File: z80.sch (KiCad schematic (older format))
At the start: 24 parts, among them J3 Conn_02x20_Odd_Even, J5 USB_B, J6 PWR, SW1 KS01Q, U1 Z80CPU, U2 74AHC14, U3 SST39SF010, U4 74AHC32, U5 AS6C1008-55PCN, U6 74AHC138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

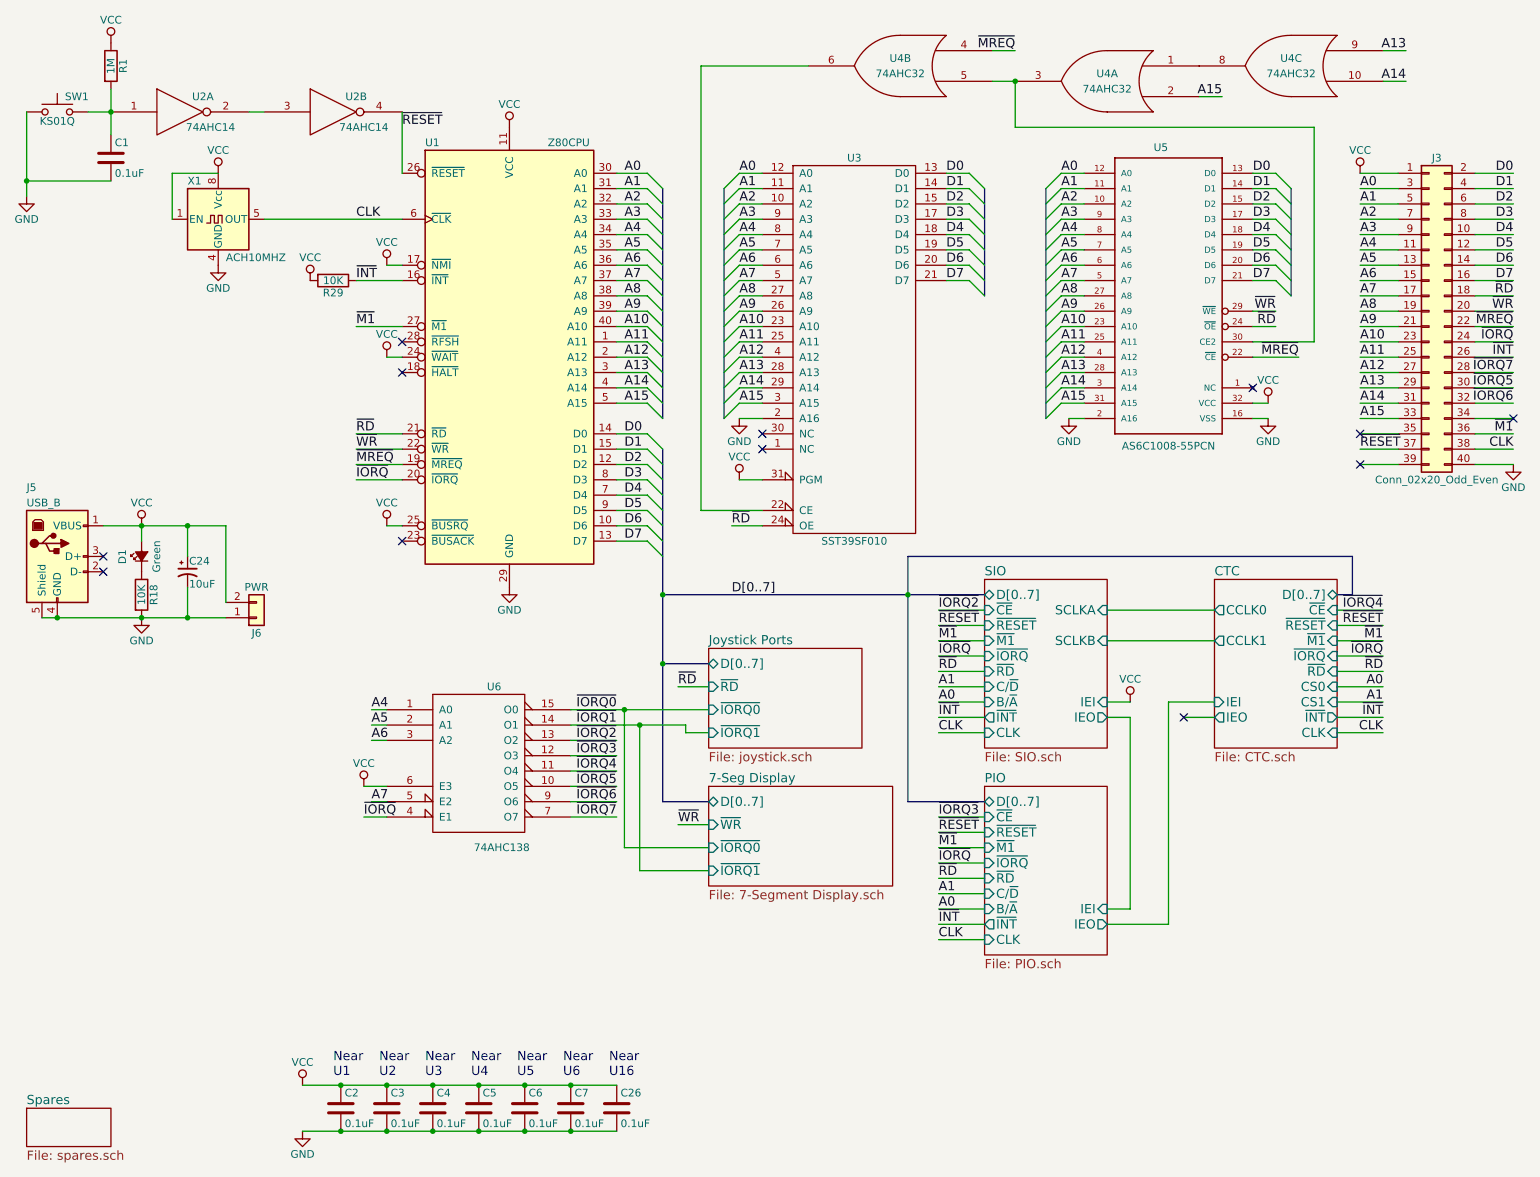
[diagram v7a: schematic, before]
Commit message: Schematic for an LCD panel interface circuit.
git-svn-id: svn+ssh://dev.thehead.ca/depot/main/z80@632 995eaefb-0ce2-40e3-b8bc-69bf8729875b
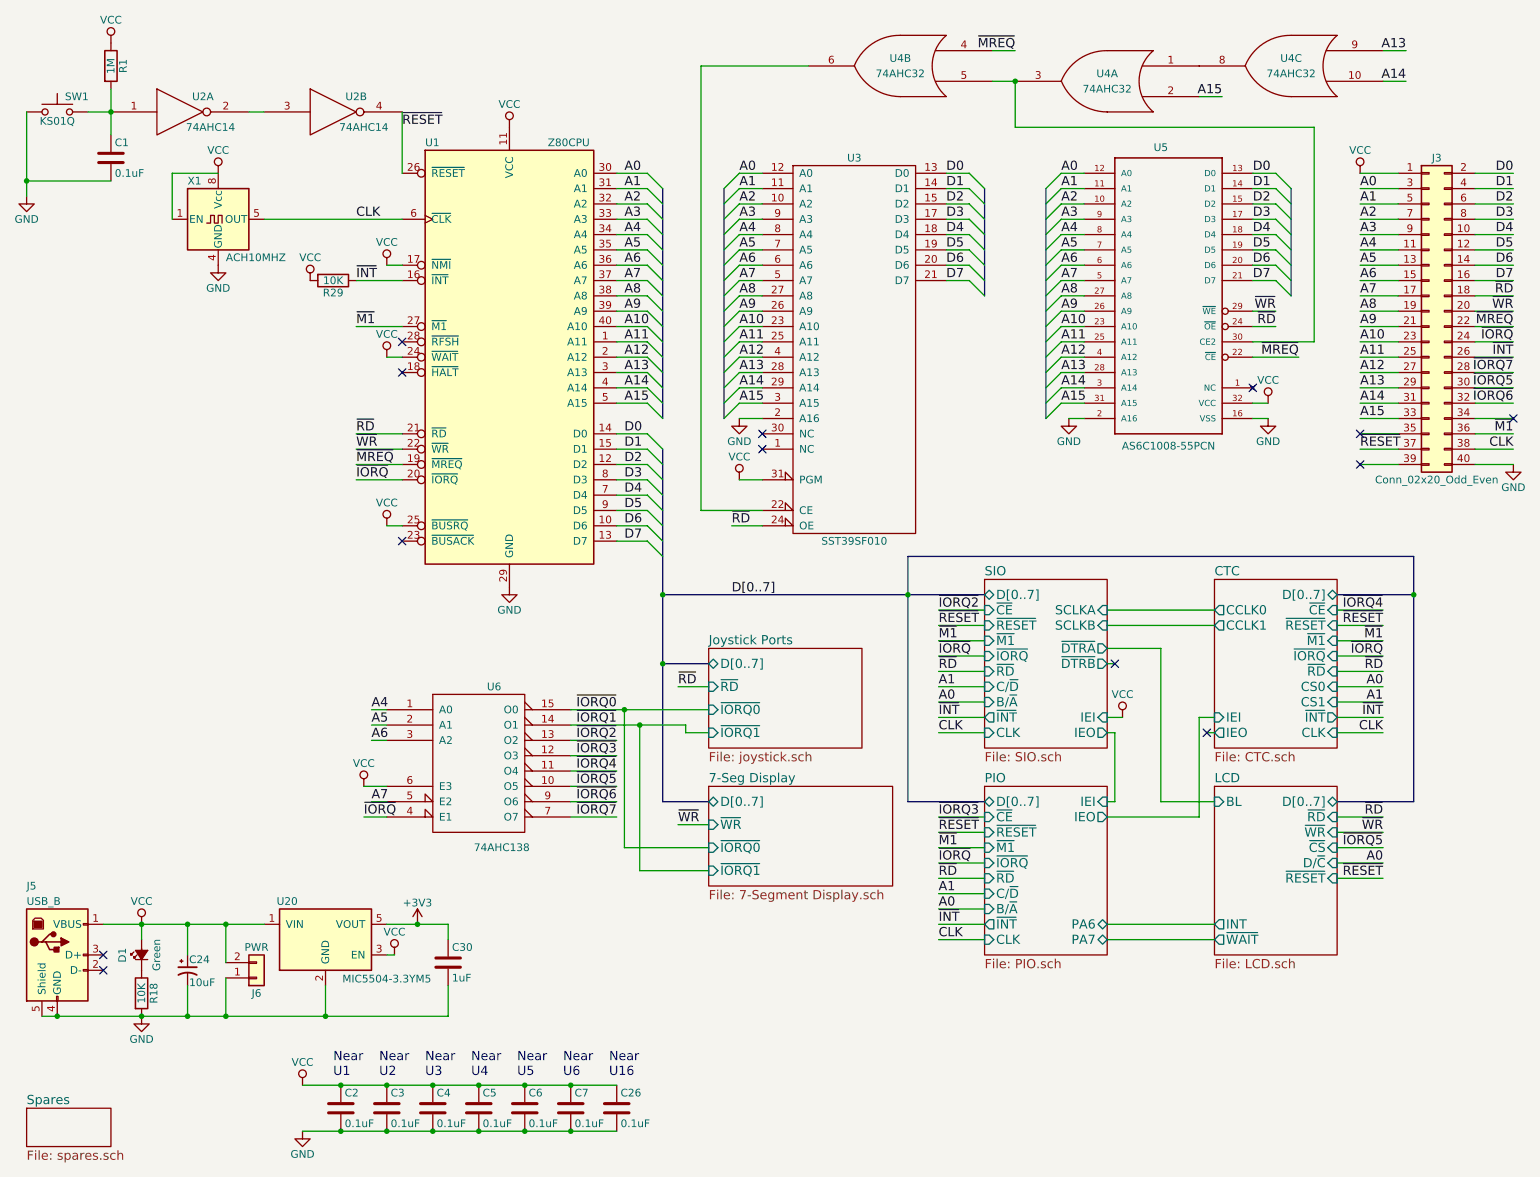
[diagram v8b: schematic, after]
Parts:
- added C30: 1uF, symbol C
- added U20: MIC5504-3.3YM5, TO_SOT_Packages_SMD:SOT-23-5, symbol MIC5504-3.3YM5
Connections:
- net GND: now also C30.2, U20.2 (GND)
- net VCC: now also U20.1 (VIN), U20.3 (EN)
- new net +3V3: C30.1, U20.5 (VOUT)
- no-connect marks 12 -> 13
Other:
- moved on the sheet: C24, D1, J5, J6, R18
